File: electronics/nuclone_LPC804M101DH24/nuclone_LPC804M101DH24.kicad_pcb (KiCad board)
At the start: 2 copper layers, 50 x 50 mm, 50 parts, among them J1 JTAG_2X05, J2 TYPE-C-31-M-12, J3 nuclone_small_left, J4 nuclone_small_right, J5 Conn_02x06_Odd_Even, SW1 RESET, SW2 Bootloader, U1 MCP1702-MB, U2 LPC804M101JHI33, U3 reference_sot23-3

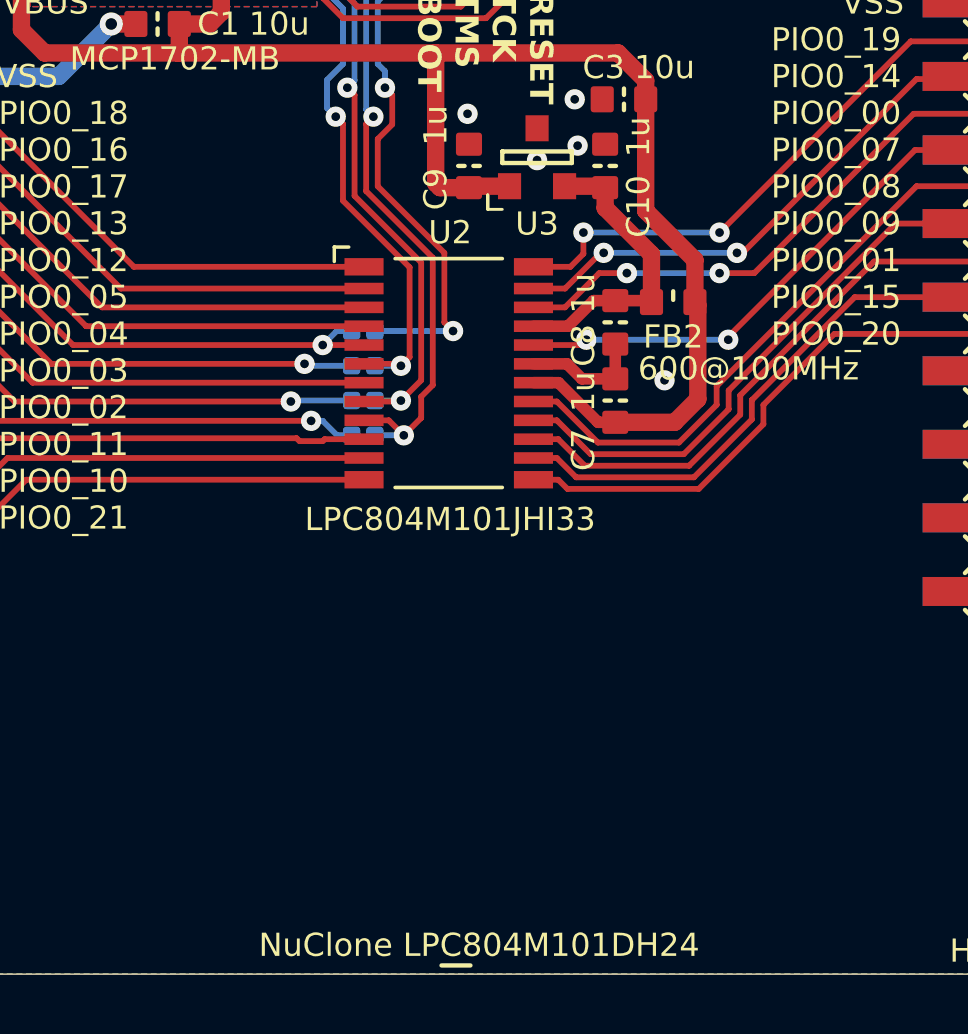
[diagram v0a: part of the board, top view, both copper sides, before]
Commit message: added crystal oscillator
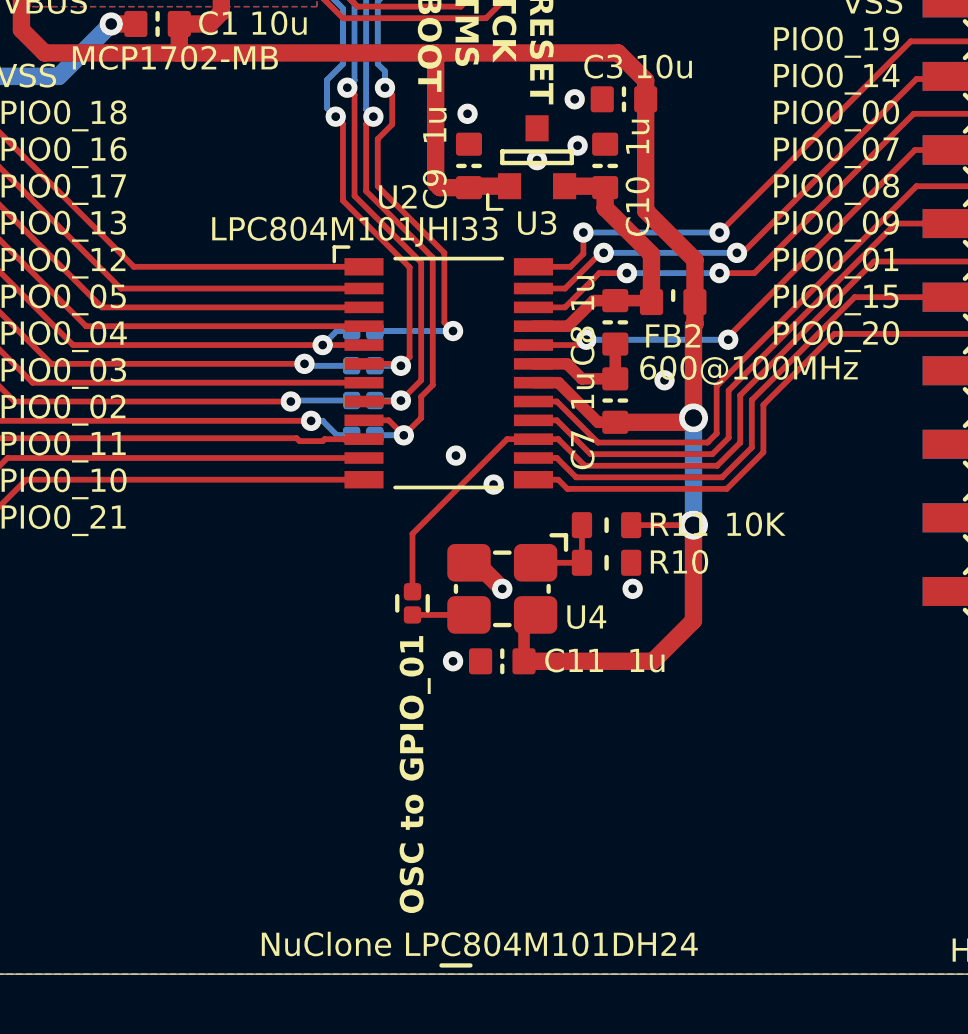
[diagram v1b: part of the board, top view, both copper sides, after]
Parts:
- added C11: 1u, SquantorCapacitor:C_0603, F.Cu at (56.8, 69.2)
- added JP5: OSC to GPIO_01, SquantorSpecial:solder_jumper_0402_2way_noconn, F.Cu at (53.7, 67.2)
- added R10: 10K, SquantorResistor:R_0603_hand, F.Cu at (60.4, 65.8)
- added R11: 10K, SquantorResistor:R_0603_hand, F.Cu at (60.4, 64.5)
- added U4: TBD, SquantorCrystal:Crystal_3225_4_hand, F.Cu at (56.8, 66.7)
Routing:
- net /VDD: track 151.9 -> 169.5 mm, vias 2 -> 4
- net /GPIO_23: track 22.9 -> 31.0 mm
- net /microcontroller/OSC_EN: track 0.00 -> 2.90 mm
- net /microcontroller/OSC_OUT: track 0.00 -> 1.95 mm
- net /VSS: track 27.8 -> 29.4 mm, vias 27 -> 32
- net /GPIO_24: track 19.2 -> 19.8 mm
- net /GPIO_25: track 23.9 -> 24.5 mm
- net /GPIO_21: track 22.0 -> 22.5 mm
- net /GPIO_22: track 18.3 -> 18.9 mm

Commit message: prepped for production with updated versionnumbers and some minor changes
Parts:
- N2: value V20240606 -> V20240712
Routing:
- net /microcontroller/VREFP: track 10.5 -> 11.2 mm, vias 0 -> 2
- net /GPIO_29: track 22.9 -> 22.4 mm, vias 2 -> 0
- net /VDD: vias 4 -> 6
- net /GPIO_27: vias 2 -> 0
- net /VSS: vias 32 -> 30
- net /GPIO_28: vias 2 -> 0
